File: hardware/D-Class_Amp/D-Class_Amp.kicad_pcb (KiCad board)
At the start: 2 copper layers, 180 x 65 mm, 99 parts, among them J101 P_IN, J102 AudioJack2, Q501 PHP23NQ11T, Q502 PHP23NQ11T, Q503 PHP23NQ11T, Q504 PHP23NQ11T, U101 NCP1117-12_TO252, U102 MCP1799T-5002H_TT, U201 LM324, U301 TL972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

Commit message: hopefully fixed the repo
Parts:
- removed the G*** at (216.7, 97.1)
- removed the G*** at (99.4, 97.3)
- added G***: LOGO, silk_art:sine, F.Cu at (99.4, 97.2)
- added G***: LOGO, silk_art:sine, F.Cu at (216.7, 97.2)
- C106: value 100u -> 100u 6.3V
- moved G*** 0.76 mm to (240.7, 98.5)
- moved G*** 0.10 mm to (98.5, 81.6)
- moved G*** 0.10 mm to (123.5, 83.6)

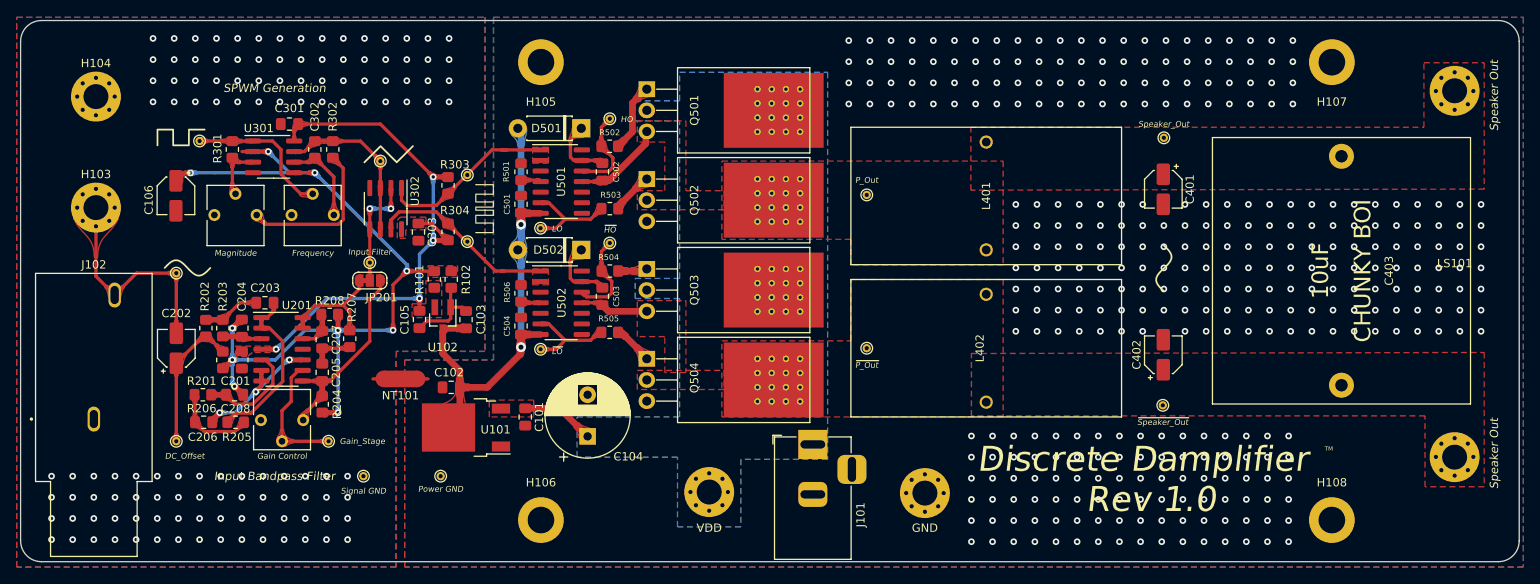
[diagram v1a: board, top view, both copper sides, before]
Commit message: rm ground planes from output zone
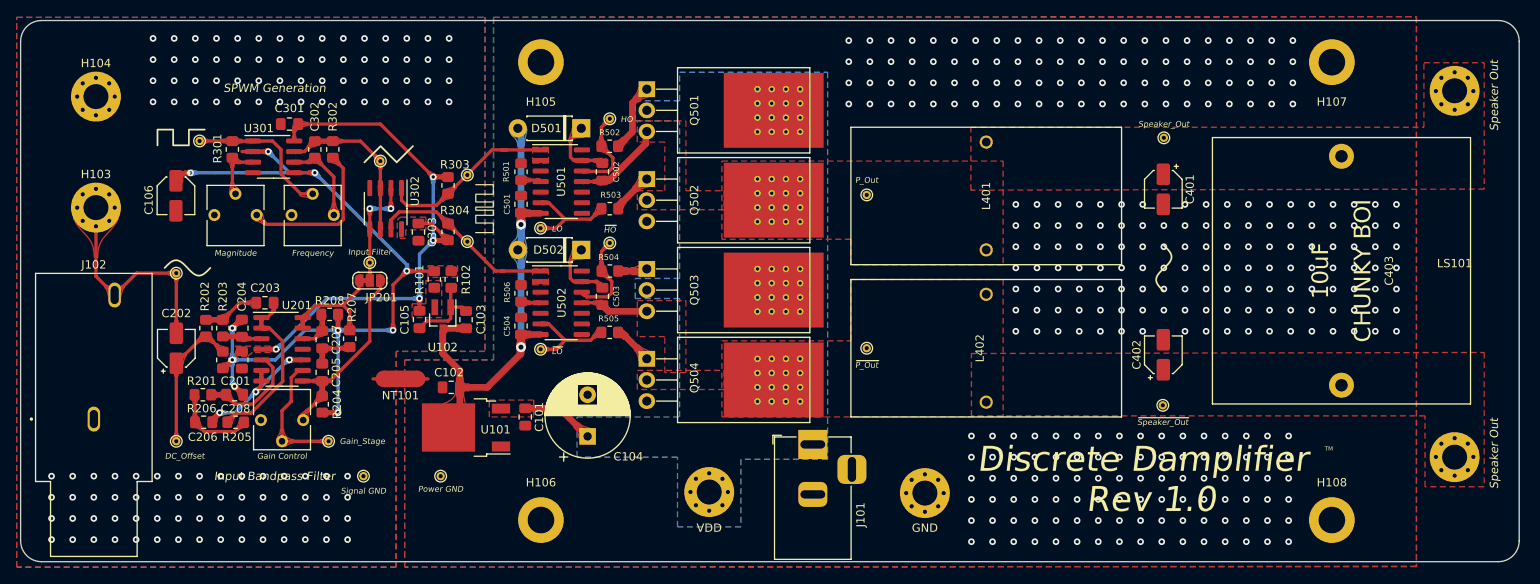
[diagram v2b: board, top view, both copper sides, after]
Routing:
- net GND: vias 343 -> 315

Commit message: fixed the inout filter gain stage
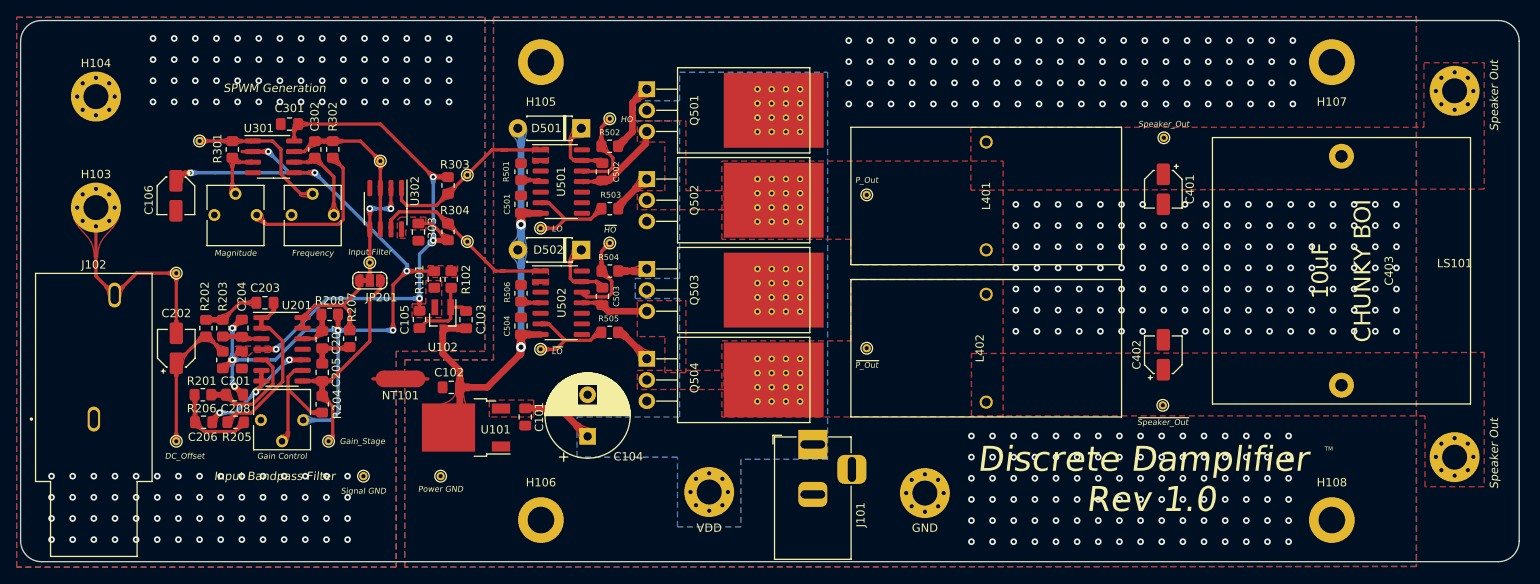
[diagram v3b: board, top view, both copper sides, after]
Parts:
- removed G***: LOGO, silk_art:thumb
- removed G***: LOGO, silk_art:triangle
- removed G***: LOGO, silk_art:square
- removed G*** (x2): LOGO, silk_art:sine
- removed G***: LOGO, silk_art:SPWM
- turned R204 to 90 degrees
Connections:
- R204 pad 1: /Input_Stage/C_OUT -> Net-(R204-Pad1)
- R204 pad 2: +2V5 -> /Input_Stage/C_OUT
- RV201 pad 2: Net-(RV201-Pad2) -> Net-(R204-Pad1)
- RV201 pad 3: /Input_Stage/C_OUT -> +2V5
- TP202 pad 1: Net-(RV201-Pad2) -> /Input_Stage/C_OUT
- U201 pad 9: Net-(RV201-Pad2) -> Net-(R204-Pad1)
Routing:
- net Net-(RV201-Pad2): track 15.4 -> 0.00 mm
- net Net-(R204-Pad1): track 0.00 -> 15.4 mm
- net +2V5: track 100.6 -> 103.2 mm, vias 10 -> 9
- net /Input_Stage/C_OUT: track 24.2 -> 26.5 mm

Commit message: update pcb and simulations of sampling
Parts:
- added G***: LOGO, silk_art:thumb, B.Cu at (241.4, 97.7)
- added G***: LOGO, silk_art:sine, F.Cu at (216.7, 97.7)
- added G***: LOGO, silk_art:SPWM, F.Cu at (134.7, 90.0)
- added G***: LOGO, silk_art:square, F.Cu at (122.6, 81.9)
- added G***: LOGO, silk_art:triangle, F.Cu at (100.8, 79.5)
- added G***: LOGO, silk_art:sine, F.Cu at (98.0, 95.8)

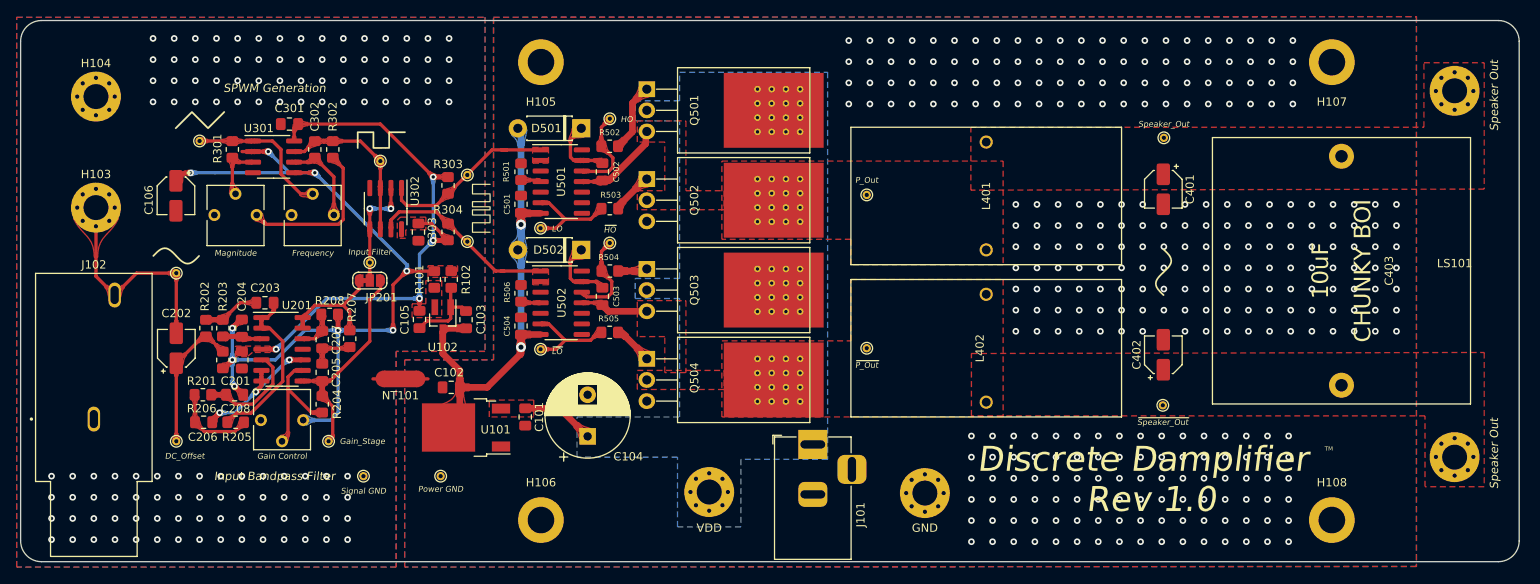
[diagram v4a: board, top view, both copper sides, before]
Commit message: added graphical symbols, exchanged THT bootstrapping diodes for SMD diodes, updated BOM
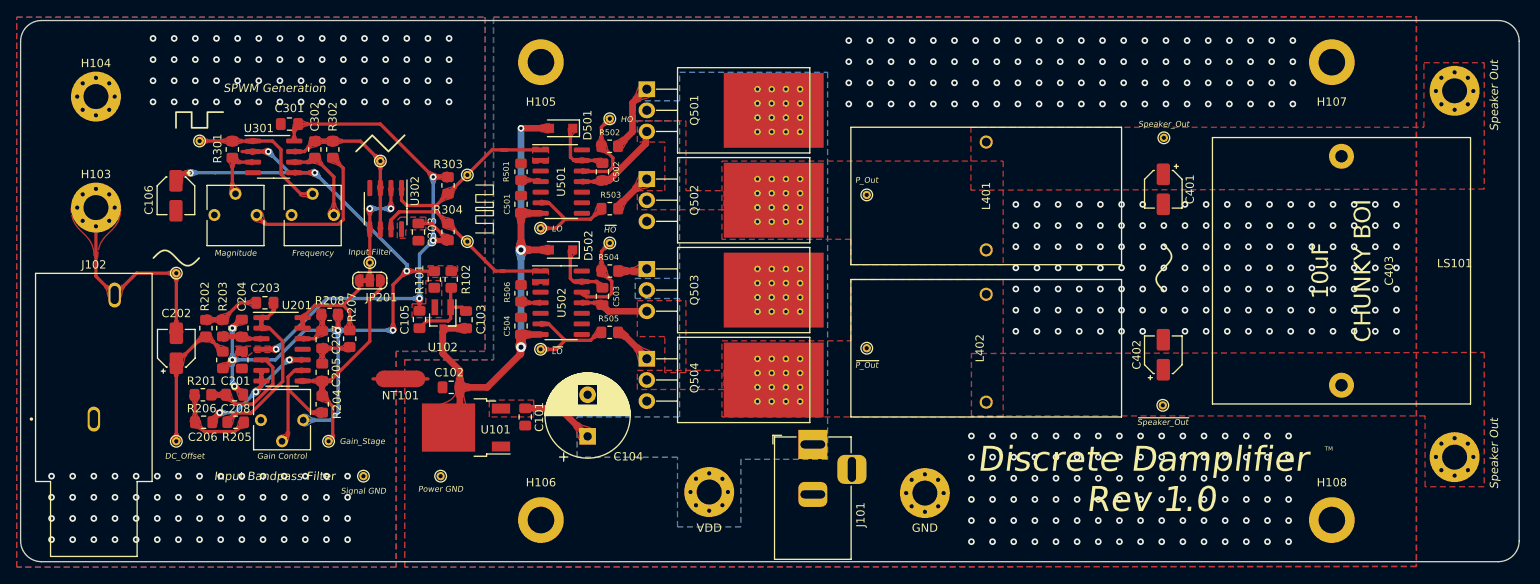
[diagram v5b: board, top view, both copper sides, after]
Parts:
- removed G***: LOGO, silk_art:thumb
- removed G*** (x2): LOGO, silk_art:sine
- removed G***: LOGO, silk_art:SPWM
- removed G***: LOGO, silk_art:square
- removed G***: LOGO, silk_art:triangle
- added G101: Input Signal, silk_art:sine, F.Cu at (98.1, 96.0)
- added G102: SPWM, silk_art:SPWM, F.Cu at (135.0, 90.0)
- added G103: Output Signal, silk_art:sine, F.Cu at (216.7, 97.1)
- added G104: Thumb, silk_art:thumb, B.Cu at (240.0, 99.1)
- added G105: Square Wave, silk_art:square, F.Cu at (100.7, 79.5)
- added G106: Triangle Wave, silk_art:triangle, F.Cu at (122.5, 82.3)
- D501, D502: value UG1B-E3/54r -> SMD1150PL-TP; footprint Diode_THT:D_DO-41_SOD81_P7.62mm_Horizontal -> Diode_SMD:D_SOD-123F
- moved D502 2.43 mm to (144.3, 95.0)
- moved D501 2.42 mm to (144.3, 80.4)
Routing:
- net +12V: track 60.8 -> 70.5 mm, vias 2 -> 3

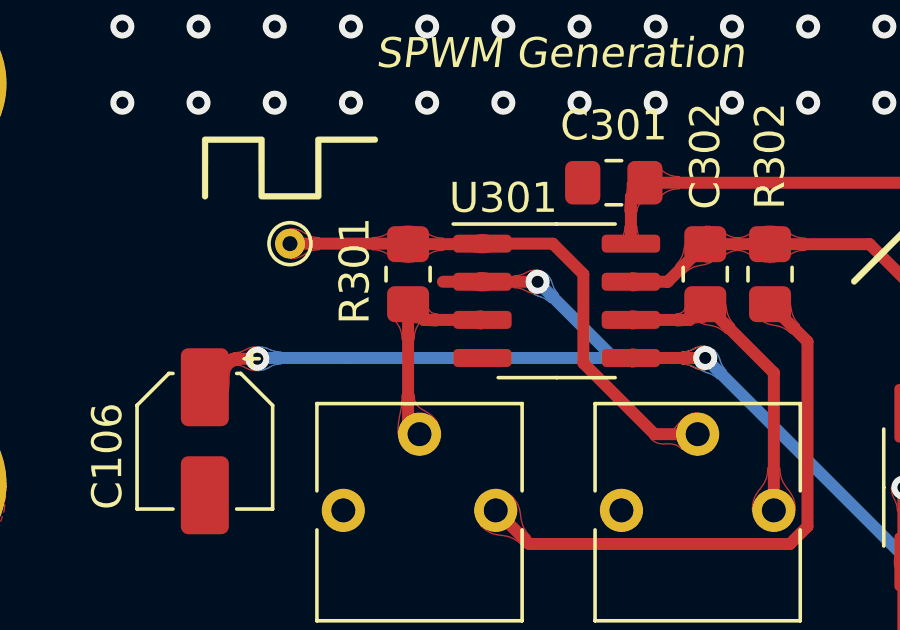
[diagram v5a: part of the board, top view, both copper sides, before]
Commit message: fixed traces extending beyond pads
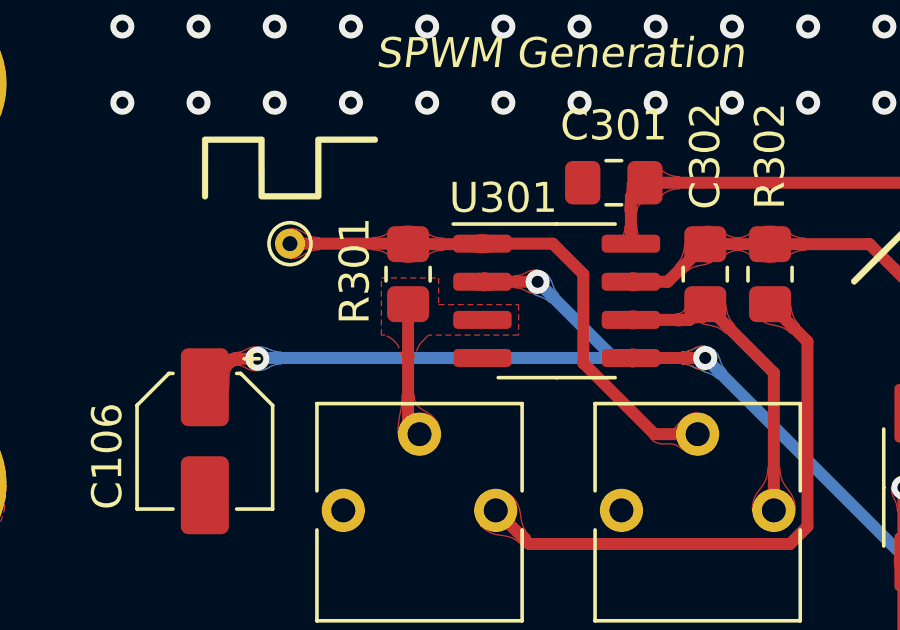
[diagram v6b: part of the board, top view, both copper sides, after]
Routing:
- net Net-(R301-Pad2): track 7.19 -> 4.49 mm
- net +2V5: track 103.2 -> 101.9 mm
- added copper zone on F.Cu, net Net-(R301-Pad2)
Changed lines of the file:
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@@
     (thickness 1.6)
     (drawings 16)
-    (tracks 748)
+    (tracks 745)
     (zones 0)
     (modules 99)
@@
     (trace_clearance 0.2)
     (zone_clearance 0.2)
-    (zone_45_only no)
+    (zone_45_only yes)
     (trace_min 0.2)
     (via_size 0.8)
@@
   (via (at 105.029 111.379) (size 0.8) (drill 0.4) (layers F.Cu B.Cu) (net 5))
   (segment (start 107.253 83.185) (end 106.685 83.185) (width 0.4) (layer F.Cu) (net 5))
-  (segment (start 107.253 83.185) (end 105.935 83.185) (width 0.4) (layer F.Cu) (net 5))
   (segment (start 111.633 85.725) (end 102.725 85.725) (width 0.4) (layer B.Cu) (net 5))
   (via (at 99.75 85.75) (size 0.8) (drill 0.4) (layers F.Cu B.Cu) (net 5))
@@
   (segment (start 104.775 87.884) (end 105.156 88.265) (width 0.4) (layer F.Cu) (net 40))
   (segment (start 104.775 83.931) (end 104.775 87.884) (width 0.4) (layer F.Cu) (net 40))
-  (segment (start 105.299 84.455) (end 104.775 83.931) (width 0.4) (layer F.Cu) (net 40))
-  (segment (start 107.253 84.455) (end 105.299 84.455) (width 0.4) (layer F.Cu) (net 40))
   (segment (start 107.237 81.931) (end 107.253 81.915) (width 0.4) (layer F.Cu) (net 41))
   (segment (start 104.775 81.931) (end 107.237 81.931) (width 0.4) (layer F.Cu) (net 41))
@@
     )
   )
+  (zone (net 40) (net_name "Net-(R301-Pad2)") (layer F.Cu) (hatch edge 0.508)
+    (priority 1)
+    (connect_pads yes (clearance 0.2))
+    (min_thickness 0.254)
+    (fill yes (arc_segments 32) (thermal_gap 0.508) (thermal_bridge_width 0.508) (smoothing fillet) (radius 0.2))
+    (polygon
+      (pts
+        (xy 105.791 83.947) (xy 108.458 83.947) (xy 108.458 84.963) (xy 105.462593 84.963) (xy 105.408208 85.009616)
+        (xy 105.3084 85.1154) (xy 105.2068 85.217) (xy 105.1306 85.3186) (xy 104.9782 85.6996) (xy 104.5718 85.6996)
+        (xy 104.4448 85.3186) (xy 104.372704 85.217) (xy 104.2416 85.09) (xy 104.013 84.963) (xy 103.886 84.963)
+        (xy 103.886 83.058) (xy 105.791 83.058)
+      )
+    )
+  )
   (zone (net 1) (net_name /Input_Stage/A_OUT) (layer F.Cu) (hatch edge 0.508)
     (priority 16962)
@@
     )
   )
-  (zone (net 5) (net_name +2V5) (layer F.Cu) (hatch edge 0.508)
-    (priority 16962)
-    (connect_pads yes (clearance 0.2))
-    (min_thickness 0.0254)
-    (fill yes (arc_segments 32) (thermal_gap 0.508) (thermal_bridge_width 0.508))
-    (polygon
-      (pts
-        (xy 106.663 83.385) (xy 106.744148 83.3878) (xy 106.810531 83.3954) (xy 106.86584 83.406599) (xy 106.913765 83.4202)
-        (xy 106.958 83.435) (xy 107.002234 83.4498) (xy 107.050159 83.4634) (xy 107.105468 83.4746) (xy 107.171851 83.4822)
-        (xy 107.253 83.485) (xy 107.403 83.185) (xy 107.253 82.885) (xy 107.171851 82.8878) (xy 107.105468 82.8954)
-        (xy 107.050159 82.906599) (xy 107.002234 82.9202) (xy 106.958 82.935) (xy 106.913765 82.9498) (xy 106.86584 82.9634)
-        (xy 106.810531 82.9746) (xy 106.744148 82.9822) (xy 106.663 82.985)
-      )
-    )
-  )
   (zone (net 5) (net_name +2V5) (layer B.Cu) (hatch edge 0.508)
     (priority 16962)
@@
       )
     )
-  )
-  (zone (net 40) (net_name "Net-(R301-Pad2)") (layer F.Cu) (hatch edge 0.508)
-    (priority 16962)
-    (connect_pads yes (clearance 0.2))
-    (min_thickness 0.0254)
-    (fill yes (arc_segments 32) (thermal_gap 0.508) (thermal_bridge_width 0.508))
-    (polygon
-      (pts
-        (xy 104.975 85.121) (xy 104.9862 84.952093) (xy 105.0166 84.816458) (xy 105.061399 84.705776) (xy 105.1158 84.611729)
-        (xy 105.175 84.526) (xy 105.2342 84.44027) (xy 105.2886 84.346223) (xy 105.3334 84.235541) (xy 105.3638 84.099906)
-        (xy 105.375 83.931) (xy 104.775 83.631) (xy 104.175 83.931) (xy 104.1862 84.099906) (xy 104.2166 84.235541)
-        (xy 104.261399 84.346223) (xy 104.3158 84.44027) (xy 104.375 84.526) (xy 104.4342 84.611729) (xy 104.4886 84.705776)
-        (xy 104.5334 84.816458) (xy 104.5638 84.952093) (xy 104.575 85.121)
-      )
-    )
-  )
-  (zone (net 40) (net_name "Net-(R301-Pad2)") (layer F.Cu) (hatch edge 0.508)
-    (priority 16962)
-    (connect_pads yes (clearance 0.2))
-    (min_thickness 0.0254)
-    (fill yes (arc_segments 32) (thermal_gap 0.508) (thermal_bridge_width 0.508))
-    (polygon
-      (pts
-        (xy 105.757952 84.255) (xy 105.637763 84.242962) (xy 105.552248 84.208875) (xy 105.493766 84.155774) (xy 105.454672 84.086696)
-        (xy 105.427324 84.004677) (xy 105.404079 83.912752) (xy 105.377293 83.81396) (xy 105.339324 83.711335) (xy 105.282528 83.607915)
-        (xy 105.199264 83.506736) (xy 104.562868 83.718868) (xy 104.775 84.531) (xy 104.909522 84.534472) (xy 105.019893 84.543896)
-        (xy 105.112151 84.557783) (xy 105.192332 84.574648) (xy 105.266476 84.593) (xy 105.340619 84.611352) (xy 105.4208 84.628216)
-        (xy 105.513058 84.642104) (xy 105.623429 84.651528) (xy 105.757952 84.655)
-      )
-    )
-  )
-  (zone (net 40) (net_name "Net-(R301-Pad2)") (layer F.Cu) (hatch edge 0.508)
-    (priority 16962)
-    (connect_pads yes (clearance 0.2))
-    (min_thickness 0.0254)
-    (fill yes (arc_segments 32) (thermal_gap 0.508) (thermal_bridge_width 0.508))
-    (polygon
-      (pts
-        (xy 106.663 84.655) (xy 106.744148 84.6578) (xy 106.810531 84.6654) (xy 106.86584 84.676599) (xy 106.913765 84.6902)
-        (xy 106.958 84.705) (xy 107.002234 84.7198) (xy 107.050159 84.7334) (xy 107.105468 84.7446) (xy 107.171851 84.7522)
-        (xy 107.253 84.755) (xy 107.403 84.455) (xy 107.253 84.155) (xy 107.171851 84.1578) (xy 107.105468 84.1654)
-        (xy 107.050159 84.176599) (xy 107.002234 84.1902) (xy 106.958 84.205) (xy 106.913765 84.2198) (xy 106.86584 84.2334)
-        (xy 106.810531 84.2446) (xy 106.744148 84.2522) (xy 106.663 84.255)
-      )
-    )
